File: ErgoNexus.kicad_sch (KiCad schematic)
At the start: 126 parts, among them SW1 SW_Push, SW2 RotaryEncoder_Switch, SW3 SW_Push, SW4 RotaryEncoder_Switch, U1 SuperMini nRF52840, U2 SuperMini nRF52840

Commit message: pinアサインの変更 Fixes #1
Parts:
- added J10, J9: Conn_01x05, Connector_PinHeader_2.54mm:PinHeader_1x05_P2.54mm_Horizontal, symbol Connector_Generic:Conn_01x05
- added J7, J8: Conn_01x02, Connector_JST:JST_PH_S2B-PH-K_1x02_P2.00mm_Horizontal, symbol Connector_Generic:Conn_01x02
- added OL7, OL8: OLED, Connector_PinSocket_2.54mm:PinSocket_1x04_P2.54mm_Vertical, symbol kbd:OLED
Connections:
- net BAT_L: now also J8.1 (Pin_1)
- net BAT_R: now also J7.1 (Pin_1)
- net GND: no longer C1.1, C2.2, C3.1, C4.2, SW1.2, SW2.C, SW2.S2, SW3.2, SW4.C, SW4.S2, U1.28 (GND), U1.3 (GND), U1.4 (GND), U2.14 (GND), U2.28 (GND), U2.3 (GND), U2.4 (GND)
- net Key0_R: no longer D28.1 (K), D31.1 (K), D34.1 (K), D37.1 (K), D41.1 (K), D45.1 (K), DI5.2 (A), DS5.2 (A), DS6.1 (K), DS7.1 (K), DS8.1 (K), RC1-4.1, RC1-5.1, RC1-6.1, RC2-4.1, RC2-5.1, RC2-6.1, RC3-4.1, RC3-5.1, RC3-6.1, RC4-5.1, RC4-6.1, RC4-7.1, RC4-8.1, RC5-5.1, RC5-6.1, RC5-7.1, RC5-8.1, RC6-5.1, RC6-6.1, RC6-7.1, RC6-8.1, U2.18 (P0.29-LF), U2.19 (P0.02-LF), U2.20 (P1.15-LF), U2.21 (P1.13-LF), U2.22 (P1.11-LF), U2.23 (P0.10-LF)
- net RoSW_L: now also U1.8 (P0.24); no longer U1.1 (P0.06)
- net RoSW_R: now also U2.8 (P0.24); no longer U2.1 (P0.06)
- net Ro_A_L: now also U1.9 (P1.00); no longer U1.5 (P0.17)
- net Ro_A_R: now also U2.9 (P1.00); no longer U2.5 (P0.17)
- net Ro_B_L: now also U1.10 (P0.11); no longer U1.6 (P0.20)
- net Ro_B_R: now also U2.10 (P0.11); no longer U2.6 (P0.20)
- net SCL_R: now reaches U2.2 (P0.08)
- net SCL_R: now also OL8.2 (SCL)
- net MOSI_R: now reaches U2.7 (P0.22)
- net MOSI_R: now also J10.3 (Pin_3)
- net SCL_L: now reaches U1.2 (P0.08)
- net SCL_L: now also OL7.2 (SCL)
- net MOSI_L: now reaches U1.7 (P0.22)
- net MOSI_L: now also J9.3 (Pin_3)
- removed net Key0_L: D10.1 (K), D13.1 (K), D17.1 (K), D21.1 (K), D4.1 (K), D7.1 (K), DI1.2 (A), DS1.1 (K), DS1.2 (A), DS2.1 (K), DS3.1 (K), DS4.1 (K), RC0-1.1, RC0-2.1, RC0-3.1, RC1-1.1, RC1-2.1, RC1-3.1, RC2-1.1, RC2-2.1, RC2-3.1, RC3-1.1, RC3-2.1, RC3-3.1, RC4-1.1, RC4-2.1, RC4-3.1, RC4-4.1, RC5-1.1, RC5-2.1, RC5-3.1, RC5-4.1, RC6-1.1, RC6-2.1, RC6-3.1, RC6-4.1, U1.17 (P0.31-LF), U1.18 (P0.29-LF), U1.19 (P0.02-LF), U1.20 (P1.15-LF), U1.21 (P1.13-LF), U1.22 (P1.11-LF), U1.23 (P0.10-LF)
- net VCC renamed EXT_VCC_L
- net EXT_VCC_L: now also J9.4 (Pin_4), OL7.3 (VCC); no longer U2.16 (3V3)
- new net: D28.1 (K), D31.1 (K), D34.1 (K), D37.1 (K), D41.1 (K), D45.1 (K), DI5.2 (A), DS5.2 (A)
- new net: D10.1 (K), D13.1 (K), D17.1 (K), D21.1 (K), D4.1 (K), D7.1 (K), DI1.2 (A), DS1.2 (A)
- new net EXT_VCC_R: J10.4 (Pin_4), OL8.3 (VCC), U2.16 (3V3)
- new net GND_L: C1.1, C2.2, J8.2 (Pin_2), J9.5 (Pin_5), OL7.4 (GND), SW1.2, SW2.C, SW2.S2, U1.28 (GND), U1.3 (GND), U1.4 (GND)
- new net GND_R: C3.1, C4.2, J10.5 (Pin_5), J7.2 (Pin_2), OL8.4 (GND), SW3.2, SW4.C, SW4.S2, U2.14 (GND), U2.28 (GND), U2.3 (GND), U2.4 (GND)
- new net Key1_R: DS6.1 (K), RC1-4.1, RC1-5.1, RC1-6.1, U2.18 (P0.29-LF)
- new net Key2_R: DS7.1 (K), RC2-4.1, RC2-5.1, RC2-6.1, U2.19 (P0.02-LF)
- new net Key3_R: DS8.1 (K), RC3-4.1, RC3-5.1, RC3-6.1, U2.20 (P1.15-LF)
- new net Key4_R: RC4-5.1, RC4-6.1, RC4-7.1, RC4-8.1, U2.21 (P1.13-LF)
- new net Key5_R: RC5-5.1, RC5-6.1, RC5-7.1, RC5-8.1, U2.22 (P1.11-LF)
- new net Key6_R: RC6-5.1, RC6-6.1, RC6-7.1, RC6-8.1, U2.23 (P0.10-LF)
- new net KeyL0: DS1.1 (K), RC0-1.1, RC0-2.1, RC0-3.1, U1.17 (P0.31-LF)
- new net KeyL1: DS2.1 (K), RC1-1.1, RC1-2.1, RC1-3.1, U1.18 (P0.29-LF)
- new net KeyL2: DS3.1 (K), RC2-1.1, RC2-2.1, RC2-3.1, U1.19 (P0.02-LF)
- new net KeyL3: DS4.1 (K), RC3-1.1, RC3-2.1, RC3-3.1, U1.20 (P1.15-LF)
- new net KeyL4: RC4-1.1, RC4-2.1, RC4-3.1, RC4-4.1, U1.21 (P1.13-LF)
- new net KeyL5: RC5-1.1, RC5-2.1, RC5-3.1, RC5-4.1, U1.22 (P1.11-LF)
- new net KeyL6: RC6-1.1, RC6-2.1, RC6-3.1, RC6-4.1, U1.23 (P0.10-LF)
- new net MISO_L: J9.2 (Pin_2), U1.6 (P0.20)
- new net MISO_R: J10.2 (Pin_2), U2.6 (P0.20)
- new net SCLK_L: J9.1 (Pin_1), U1.5 (P0.17)
- new net SCLK_R: J10.1 (Pin_1), U2.5 (P0.17)
- new net SDA_L: OL7.1 (SDA), U1.1 (P0.06)
- new net SDA_R: OL8.1 (SDA), U2.1 (P0.06)
- no-connect marks 20 -> 10
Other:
- moved on the sheet: D1, D10, D11, D12, D13, D14, D15, D16, D17, D18, D19, D2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

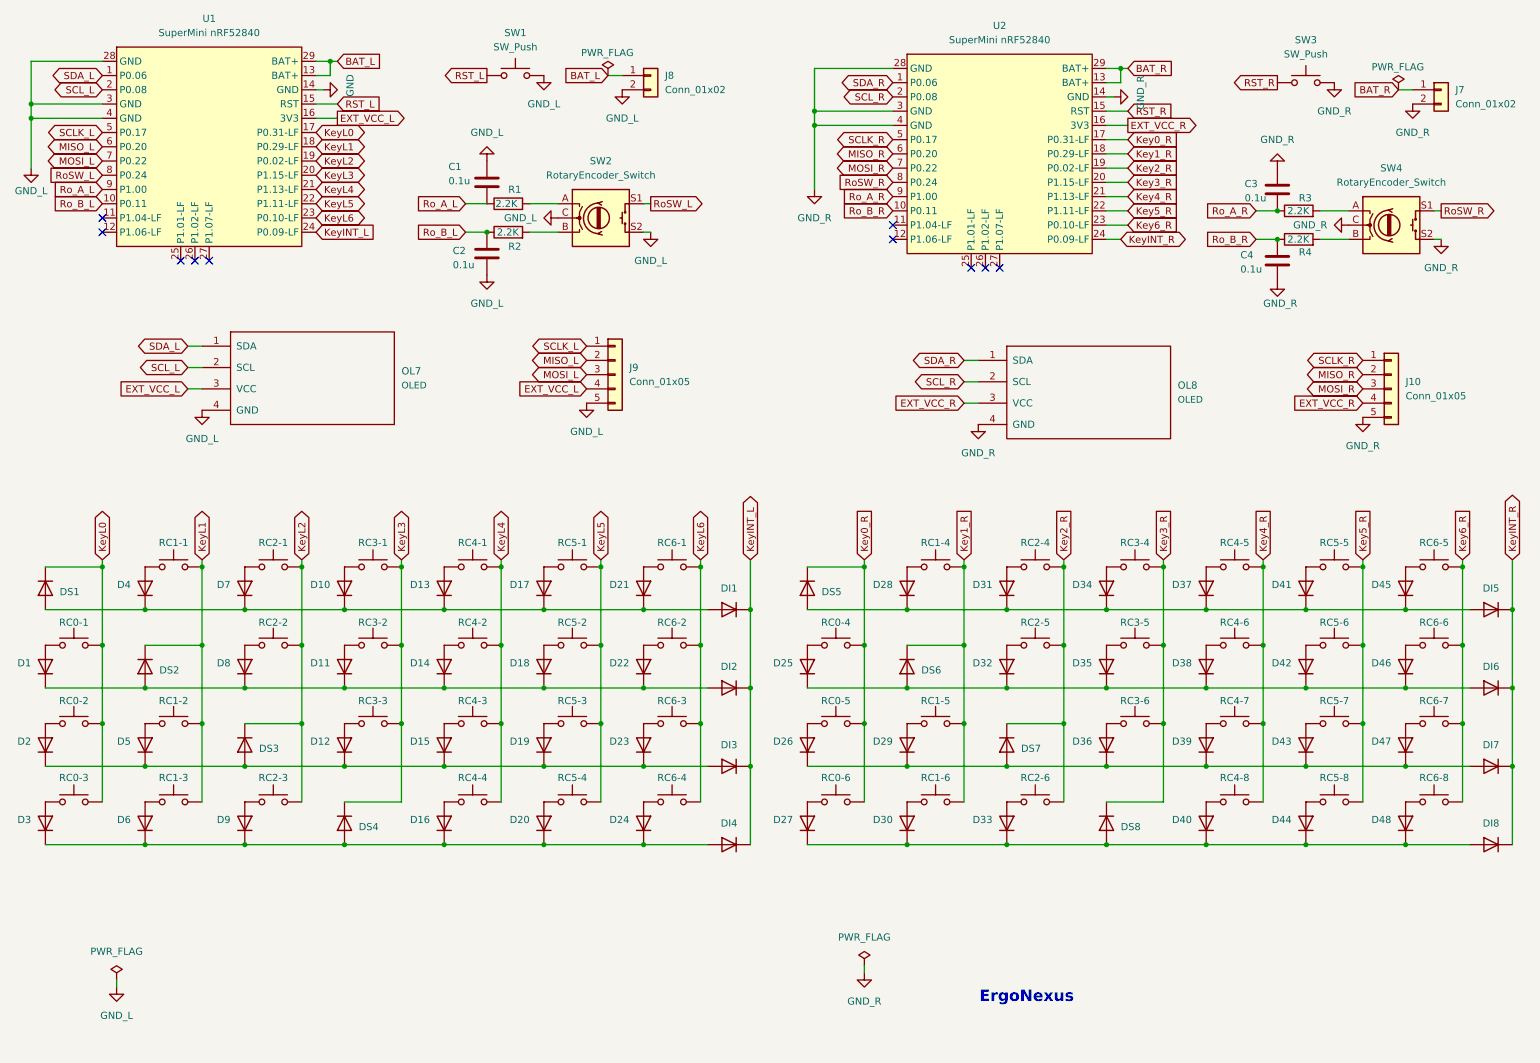
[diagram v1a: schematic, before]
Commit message: fix: forget spi cs pin
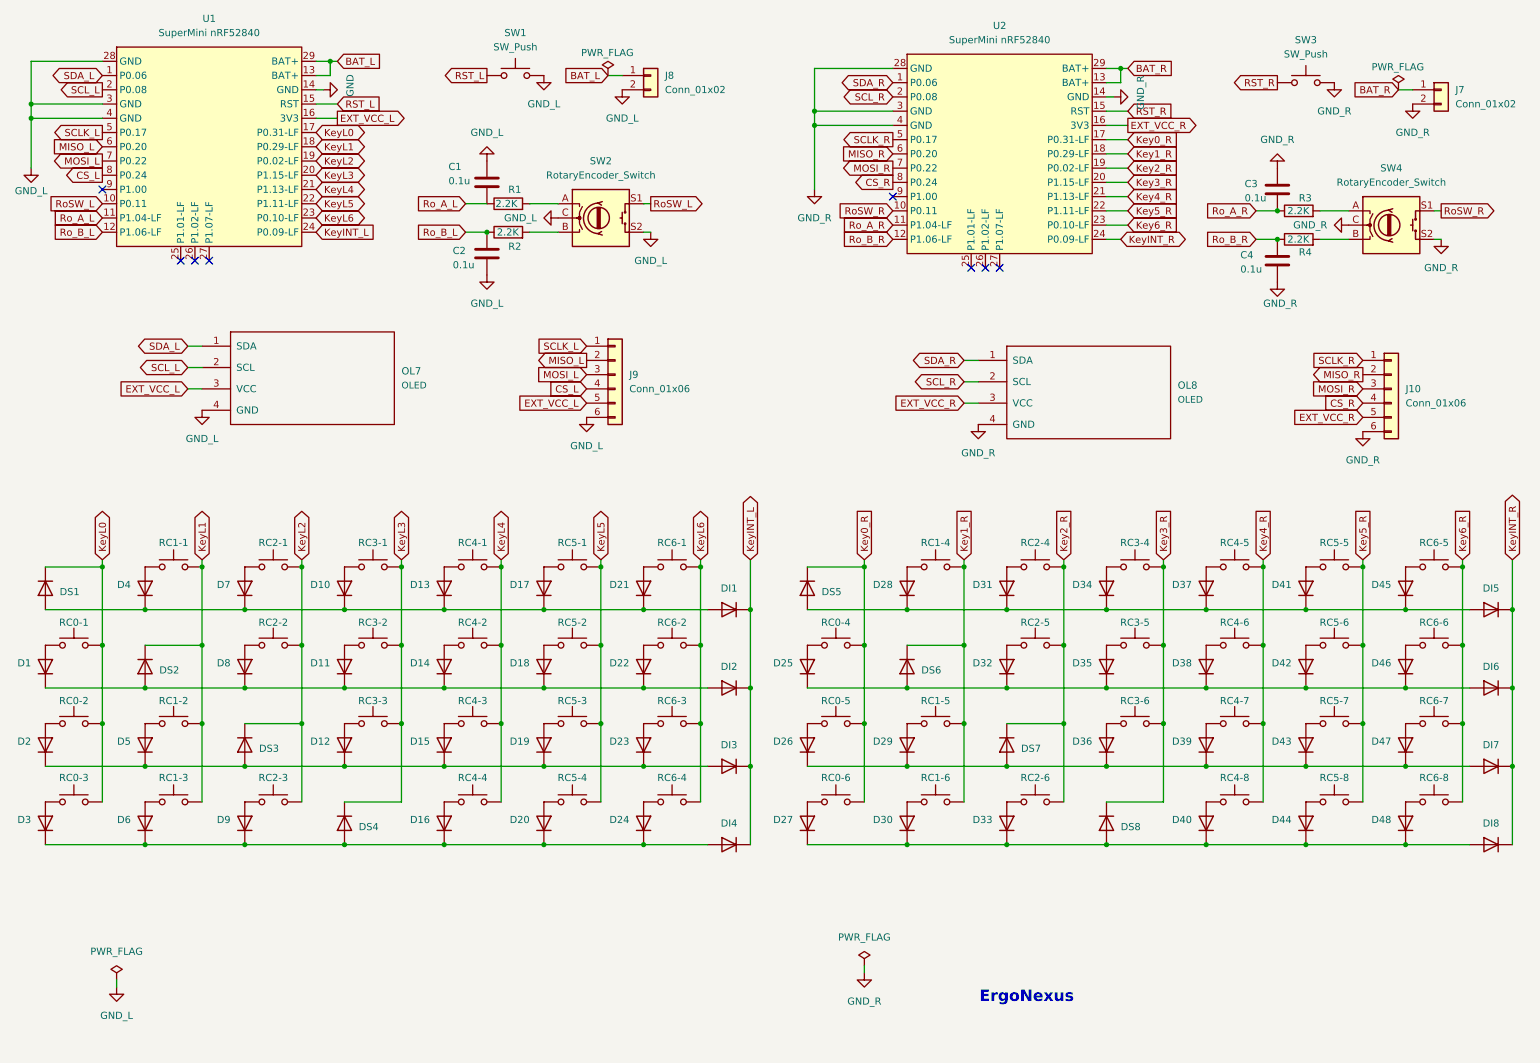
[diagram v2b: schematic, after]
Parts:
- J10, J9: value Conn_01x05 -> Conn_01x06; footprint Connector_PinHeader_2.54mm:PinHeader_1x05_P2.54mm_Horizontal -> Connector_PinHeader_2.54mm:PinHeader_1x06_P2.54mm_Horizontal; symbol Connector_Generic:Conn_01x05 -> Connector_Generic:Conn_01x06
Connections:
- net EXT_VCC_L: now also J9.5 (Pin_5); no longer J9.4 (Pin_4)
- net EXT_VCC_R: now also J10.5 (Pin_5); no longer J10.4 (Pin_4)
- net GND_L: now also J9.6 (Pin_6); no longer J9.5 (Pin_5)
- net GND_R: now also J10.6 (Pin_6); no longer J10.5 (Pin_5)
- net RoSW_L: now also U1.10 (P0.11); no longer U1.8 (P0.24)
- net RoSW_R: now also U2.10 (P0.11); no longer U2.8 (P0.24)
- net Ro_A_L: now also U1.11 (P1.04-LF); no longer U1.9 (P1.00)
- net Ro_A_R: now also U2.11 (P1.04-LF); no longer U2.9 (P1.00)
- net Ro_B_L: now also U1.12 (P1.06-LF); no longer U1.10 (P0.11)
- net Ro_B_R: now also U2.12 (P1.06-LF); no longer U2.10 (P0.11)
- new net CS_L: J9.4 (Pin_4), U1.8 (P0.24)
- new net CS_R: J10.4 (Pin_4), U2.8 (P0.24)
- no-connect marks 10 -> 8
